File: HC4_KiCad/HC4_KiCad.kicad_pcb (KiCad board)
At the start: 2 copper layers, 150 x 175 mm, 164 parts, among them IC1 RAM, IC10 74HC4002, IC11 74HC161, IC12 74HC377, IC13 74HC161, IC14 74HC161, IC15 74HC161, IC16 74HC257, IC17 74HC257, IC18 74HC32, IC19 74HC74, IC2 ROM, IC20 74HC00, IC21 74HC4053, IC22 74HC04, IC23 74HC151, IC24 74HC14, IC3 74HC153, IC4 74HC153, IC5 74HC153, IC6 74HC153, IC7 74HC283, IC8 74HC257, IC9 74HC244, J1 Power, J2 CE, J3 Expantion_Connector, SW1 SW_SPDT, SW2 Bus_Open, SW3 SW_Push, SW4 SW_Push, SW5 SW_SPDT

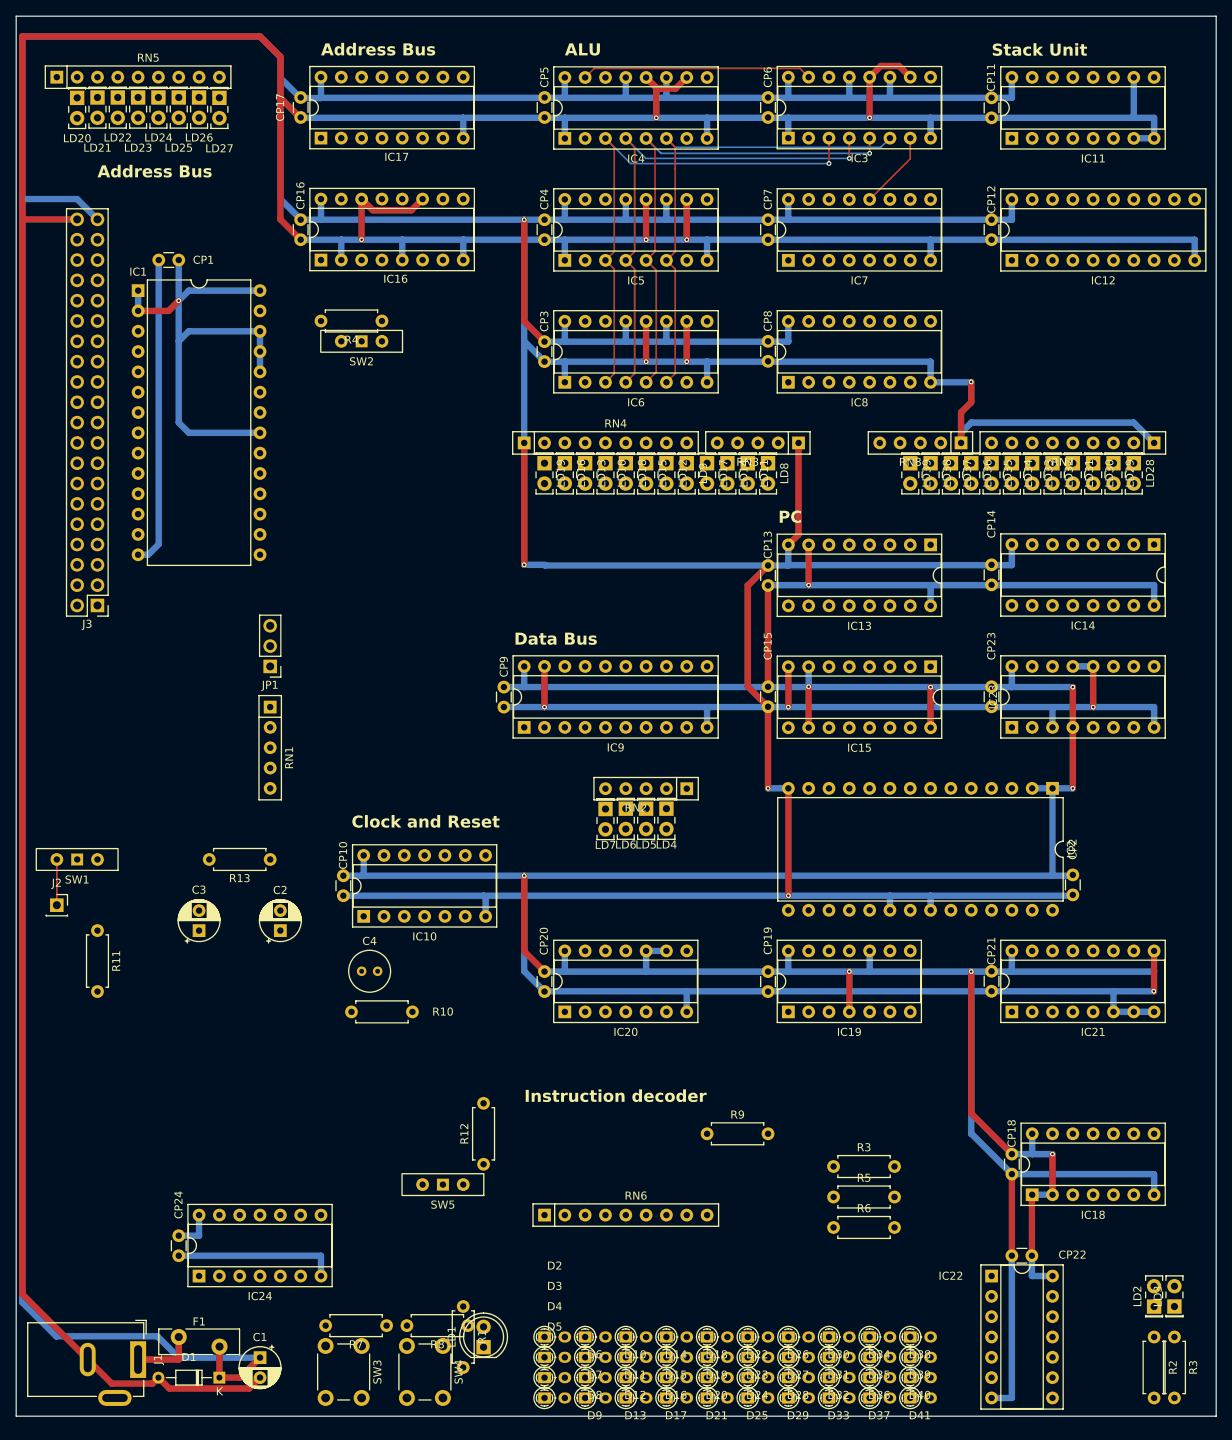
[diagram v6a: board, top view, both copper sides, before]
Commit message: ALUとスタックの配線完了
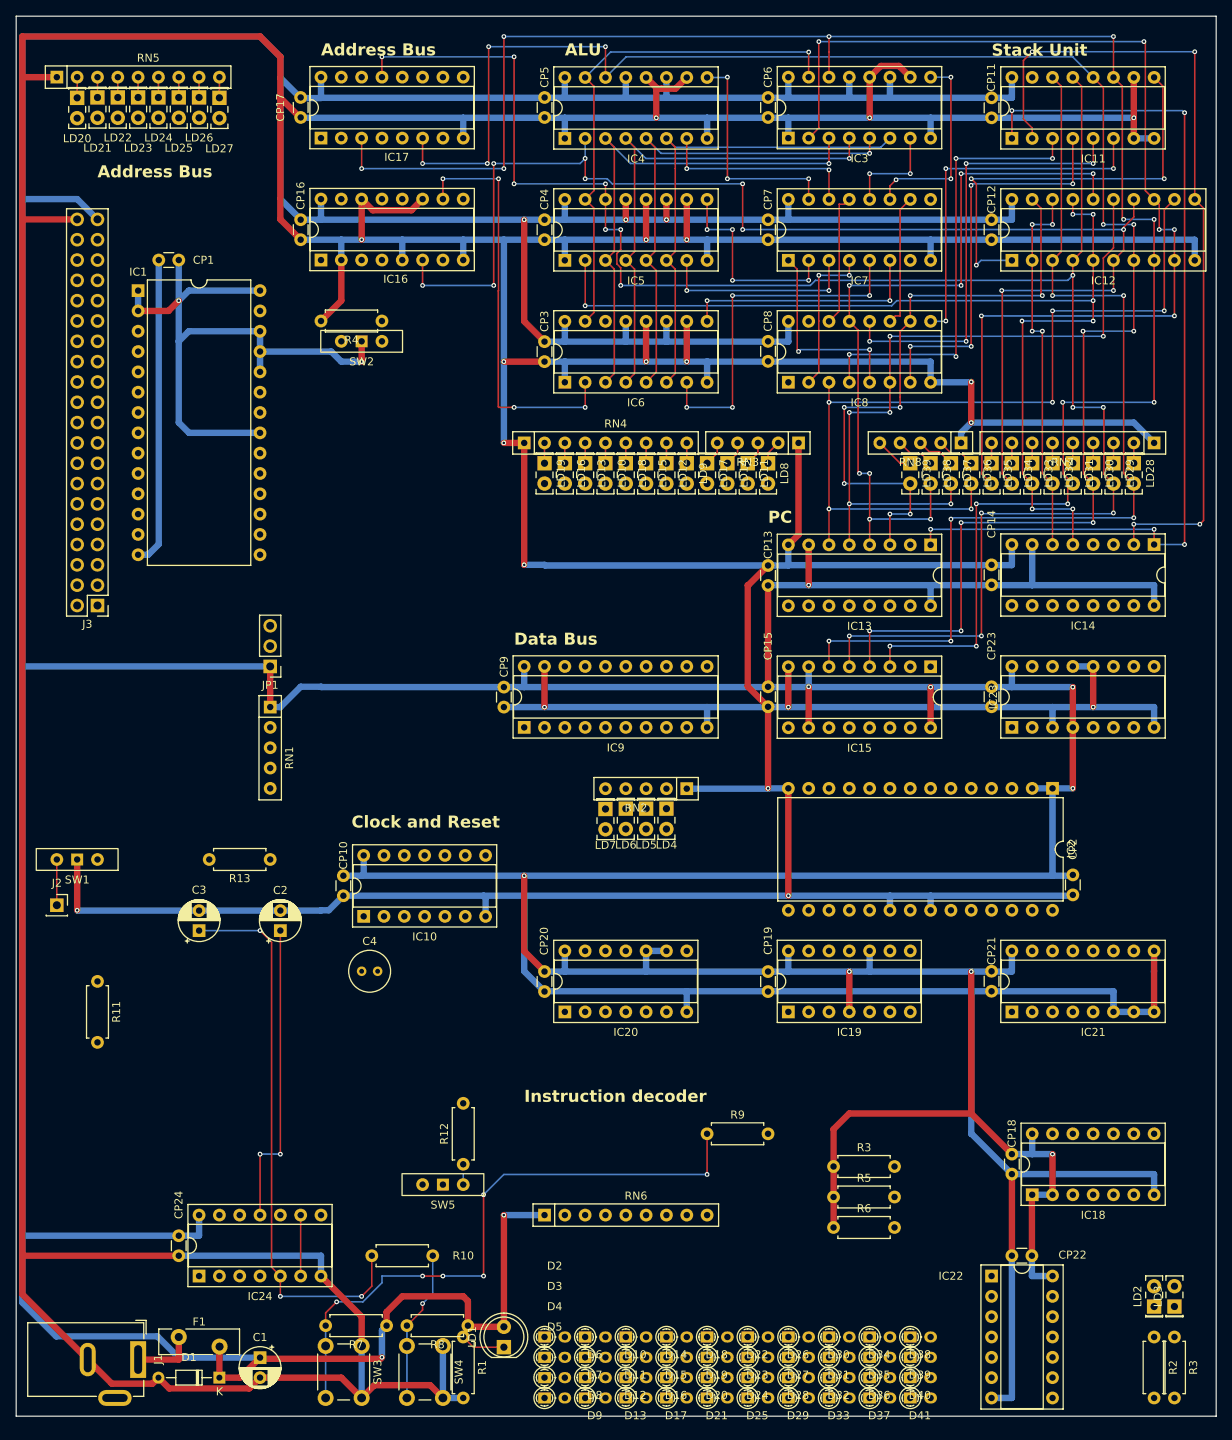
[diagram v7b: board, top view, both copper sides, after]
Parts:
- moved R10 30.6 mm to (143.5, 177.8)
- moved R11 6.35 mm to (101.6, 143.5)
- moved R1 3.81 mm to (147.3, 188.0)
- moved R12 2.54 mm to (147.3, 166.4)
- moved LD1 2.54 mm to (152.4, 189.2)
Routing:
- net /ALU/ALU_in_A3: track 0.00 -> 236.9 mm, vias 0 -> 13
- net /ALU/ALU_in_A1: track 0.00 -> 230.4 mm, vias 0 -> 14
- net /ALU/ALU_in_A2: track 0.00 -> 220.3 mm, vias 0 -> 12
- net VCC: track 1055.9 -> 1234.2 mm, vias 11 -> 16
- net /ALU/ALU_in_B2: track 0.00 -> 168.4 mm, vias 0 -> 10
- net /ALU/ALU_in_B3: track 0.00 -> 135.8 mm, vias 0 -> 6
- net GND: track 1284.7 -> 1415.1 mm, vias 15 -> 19
- net /ALU/ALU_in_B1: track 0.00 -> 129.6 mm, vias 0 -> 8
- net /ALU/ALU_in_A0: track 0.00 -> 122.0 mm, vias 0 -> 6
- net ~{RESET}: track 0.00 -> 114.7 mm, vias 0 -> 5
- net /Data BUS/Level_C0: track 0.00 -> 109.1 mm, vias 0 -> 6
- net CLK: track 0.00 -> 102.6 mm, vias 0 -> 4
- net /ALU/ALU_in_B0: track 0.00 -> 99.5 mm, vias 0 -> 8
- net /Data BUS/Level_C2: track 0.00 -> 94.0 mm, vias 0 -> 8
- net /Data BUS/Level_C1: track 0.00 -> 90.7 mm, vias 0 -> 6
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
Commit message: 上半分の配線だいたい終わった
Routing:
- net /Address BUS/Instruction_7: track 0.00 -> 300.0 mm, vias 0 -> 11
- net /Address BUS/Instruction_0: track 0.00 -> 252.7 mm, vias 0 -> 9
- net /Address BUS/Instruction_1: track 0.00 -> 229.1 mm, vias 0 -> 8
- net /Address BUS/MEMMode: track 0.00 -> 198.3 mm, vias 0 -> 2
- net /ALU/I2a: track 63.8 -> 257.7 mm, vias 1 -> 7
- net /ALU/I3a: track 64.7 -> 251.3 mm, vias 1 -> 7
- net /Instruction Decoder/Carry_Flg: track 0.00 -> 178.4 mm, vias 0 -> 4
- net /Address BUS/Instruction_3: track 0.00 -> 155.6 mm, vias 0 -> 6
- net /Instruction Decoder/~{STACK_LE}: track 53.1 -> 206.7 mm, vias 3 -> 7
- net /ALU/ALU_in_B3: track 135.8 -> 286.8 mm, vias 6 -> 13
- net /Data BUS/Level_C_OE: track 0.00 -> 143.5 mm, vias 0 -> 2
- net /ALU/ALU_in_A0: track 122.0 -> 259.8 mm, vias 6 -> 10
- net /ALU/Carry_OUT: track 0.00 -> 135.1 mm, vias 0 -> 4
- net /ALU/I0a: track 61.2 -> 191.7 mm, vias 0 -> 2
- net /Address BUS/Instruction_5: track 0.00 -> 123.7 mm, vias 0 -> 3
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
